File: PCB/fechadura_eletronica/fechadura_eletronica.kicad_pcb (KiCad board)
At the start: 2 copper layers, 12 parts, among them J1 Relay Module, J2 RFID - RC522, J3 LCD 16X2, J4 DY50, SW1 reset button, U1 LM7805 - regulator, U2 ESP32-DEVKIT-V1

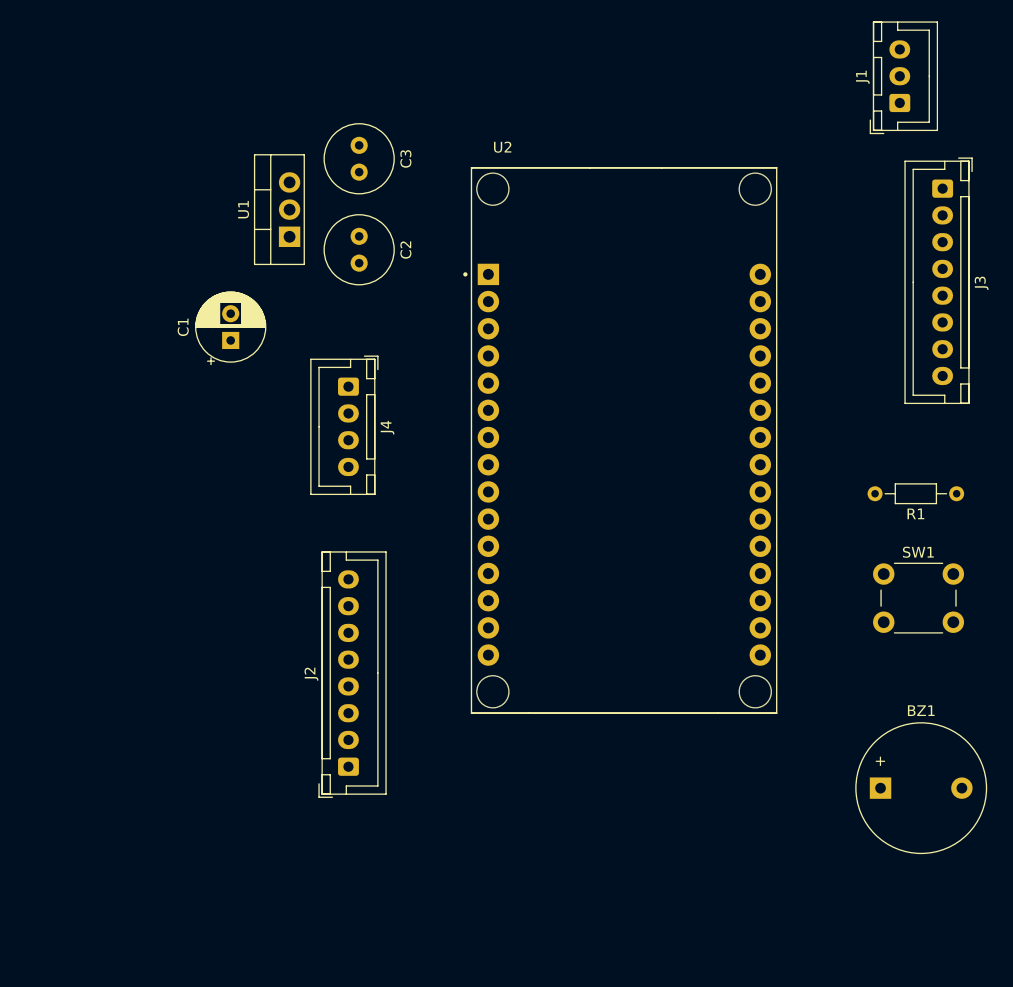
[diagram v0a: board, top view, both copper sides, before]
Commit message: feito o roteamento das trilhas da PCB
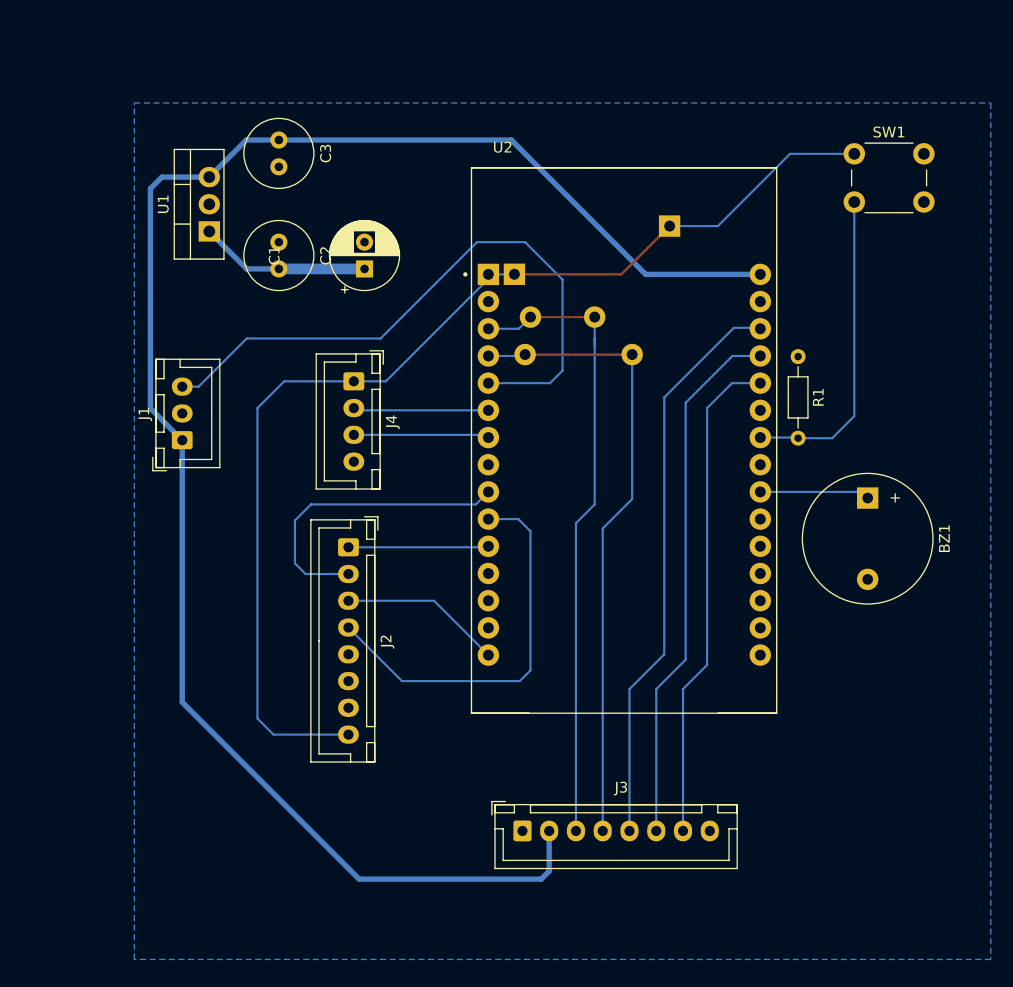
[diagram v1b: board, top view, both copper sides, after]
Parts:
- added ?: , , F.Cu at (130.0, 46.5)
- added ?: , , F.Cu at (126.5, 58.5)
- added ?: , , F.Cu at (116.5, 58.5)
- added ?: , , F.Cu at (123.0, 55.0)
- added ?: , , F.Cu at (115.5, 51.0)
- added ?: , , F.Cu at (117.0, 55.0)
- moved J1 74.1 mm to (84.5, 66.5)
- moved J3 71.7 mm to (116.2, 103.0), turned to 0 degrees
- moved SW1 39.3 mm to (147.2, 39.8)
- moved BZ1 27.1 mm to (148.5, 71.9), turned to -90 degrees
- moved J2 20.5 mm to (100.0, 76.5), turned to -90 degrees
- moved R1 19.6 mm to (142.0, 58.7), turned to -90 degrees
- moved C1 14.2 mm to (101.5, 50.5)
- moved C2 7.52 mm to (93.5, 48.0)
- moved C3 7.52 mm to (93.5, 38.5)
- moved U1 7.52 mm to (87.0, 47.0)
- moved J4 0.71 mm to (100.5, 61.0)
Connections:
- J3 pad 2: +3.3V -> +5V
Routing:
- net +5V: track 0.00 -> 158.4 mm
- net +3.3V: track 0.00 -> 104.0 mm
- net Net-(J3-RS): track 0.00 -> 59.9 mm
- net Net-(J3-E): track 0.00 -> 59.1 mm
- net Net-(J1-IN): track 0.00 -> 58.5 mm
- net Net-(J3-D4): track 0.00 -> 53.5 mm
- net Net-(J3-D5): track 0.00 -> 49.9 mm
- net Net-(J3-D6): track 0.00 -> 46.4 mm
- net Net-(J2-MISO): track 0.00 -> 36.9 mm
- net Net-(U2-D26): track 0.00 -> 29.8 mm
- net Net-(J2-SCK): track 0.00 -> 28.6 mm
- net +12V: track 0.00 -> 15.9 mm
- net Net-(J2-MOSI): track 0.00 -> 15.2 mm
- net Net-(J2-SDA): track 0.00 -> 13.1 mm
- net Net-(J4-RX): track 0.00 -> 12.7 mm
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- added copper zone on B.Cu, net GND

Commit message: adicionado regulador 3.3v LD1117 e PCB refatorada
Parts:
- added C4: C, Capacitor_THT:C_Radial_D6.3mm_H7.0mm_P2.50mm, F.Cu at (93.8, 49.5)
- added C5: C, Capacitor_THT:C_Radial_D6.3mm_H7.0mm_P2.50mm, F.Cu at (93.8, 41.8)
- added U3: LD1117S33TR_SOT223, Package_TO_SOT_THT:TO-220-3_Vertical, F.Cu at (86.8, 47.1)
- moved U1 61.8 mm to (86.3, 108.8)
- moved C3 61.8 mm to (92.8, 100.2)
- moved C2 60.3 mm to (93.0, 108.3)
- moved C1 35.6 mm to (78.5, 77.7), turned to 0 degrees
- moved BZ1 31.4 mm to (148.7, 103.3), turned to 180 degrees
- moved SW1 2.80 mm to (144.4, 39.8)
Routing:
- net +12V: track 15.9 -> 120.2 mm
- net +5V: track 158.4 -> 76.6 mm
- net +3.3V: track 104.0 -> 150.6 mm
- net Net-(J3-D7): track 0.00 -> 42.7 mm
- net Net-(BZ1-+): track 10.3 -> 37.5 mm
- net Net-(J1-IN): track 58.5 -> 61.0 mm
- net Net-(U2-D26): track 29.8 -> 27.8 mm
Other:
- board outline added: 85 x 82.7 mm
